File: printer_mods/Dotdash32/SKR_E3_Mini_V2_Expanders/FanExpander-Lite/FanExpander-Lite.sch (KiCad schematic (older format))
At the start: 31 parts, among them J1 FAN1, J2 FAN2, J3 FAN3, J4 FAN4, J5 EXP1_IN, J6 FAN1_IN, J7 IO_PassThrough, Q1 IRLML6344, Q2 IRLML6344, Q3 IRLML6344

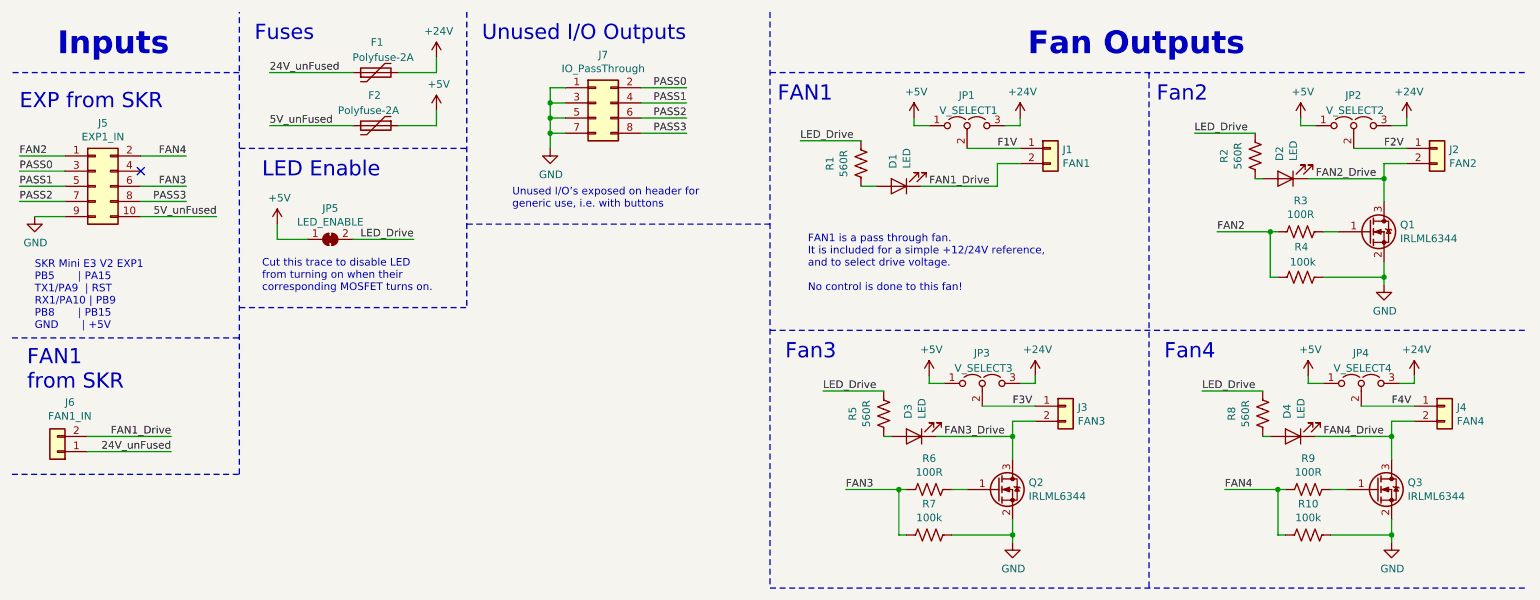
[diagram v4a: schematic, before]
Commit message: feat: trim outline to not collide with TH exp
also some fun little changes for internal structure
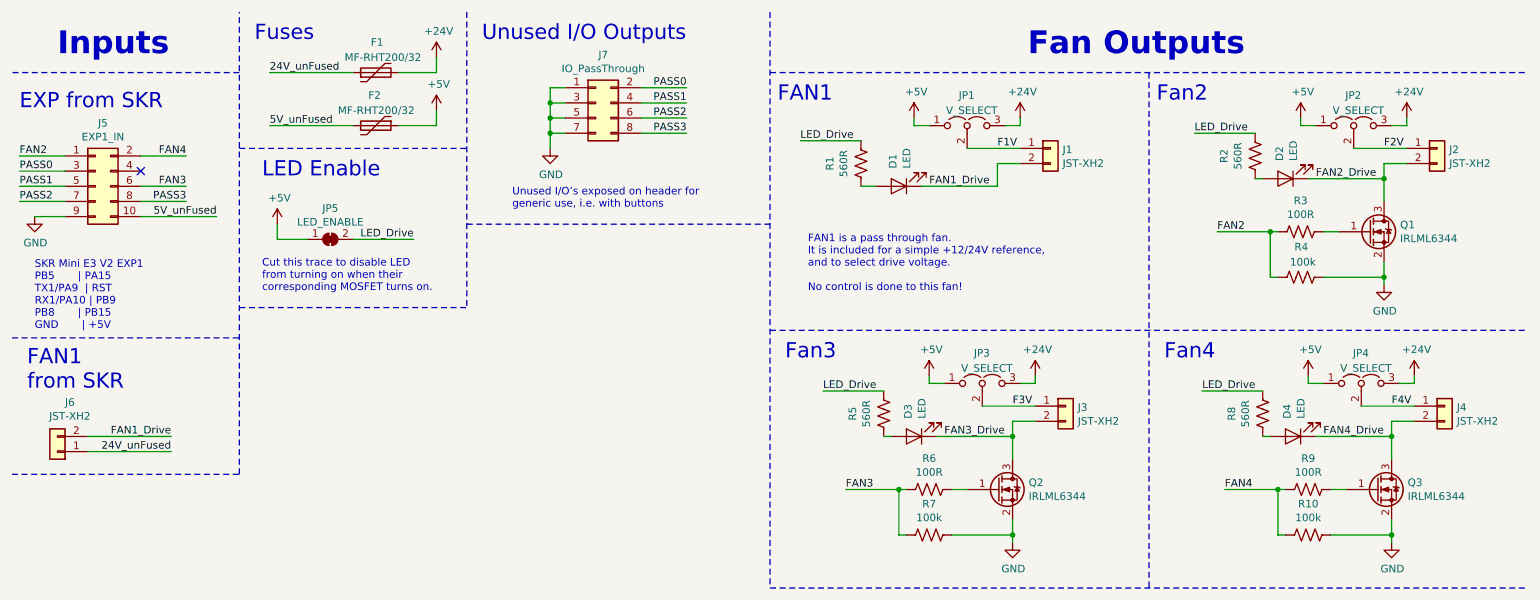
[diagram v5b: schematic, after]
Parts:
- F1, F2: value Polyfuse-2A -> MF-RHT200/32
- J1: value FAN1 -> JST-XH2
- J2: value FAN2 -> JST-XH2
- J3: value FAN3 -> JST-XH2
- J4: value FAN4 -> JST-XH2
- J6: value FAN1_IN -> JST-XH2
- JP1: value V_SELECT1 -> V_SELECT
- JP2: value V_SELECT2 -> V_SELECT
- JP3: value V_SELECT3 -> V_SELECT
- JP4: value V_SELECT4 -> V_SELECT
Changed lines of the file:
@@
 Sheet 1 1
 Title "SKR E3 Mini Fan Expander Lite"
-Date "2021-12-18"
-Rev "V0.1.1"
+Date "2022-01-05"
+Rev "V1.0.1"
 Comp "Voron Design"
 Comment1 "Drawn by Dotdash32 (JDeW)"
@@
 P 800 3400
 F 0 "J6" H 718 3075 50  0000 C CNN
-F 1 "FAN1_IN" H 718 3166 50  0000 C CNN
+F 1 "JST-XH2" H 718 3166 50  0000 C CNN
 F 2 "Connectors_JST:JST_XH_B02B-XH-A_02x2.50mm_Straight" H 800 3400 50  0001 C CNN
 F 3 "~" H 800 3400 50  0001 C CNN
@@
 P 2900 900
 F 0 "F1" V 3100 850 50  0000 L CNN
-F 1 "Polyfuse-2A" V 3000 650 50  0000 L CNN
+F 1 "MF-RHT200/32" V 3000 600 50  0000 L CNN
 F 2 "Fuse:Fuse_Bourns_MF-RHT200" H 2950 700 50  0001 L CNN
 F 3 "~" H 2900 900 50  0001 C CNN
@@
 P 7350 1400
 F 0 "J1" H 7430 1392 50  0000 L CNN
-F 1 "FAN1" H 7430 1301 50  0000 L CNN
+F 1 "JST-XH2" H 7430 1301 50  0000 L CNN
 F 2 "Connectors_JST:JST_XH_B02B-XH-A_02x2.50mm_Straight" H 7350 1400 50  0001 C CNN
 F 3 "~" H 7350 1400 50  0001 C CNN
@@
 P 6800 1250
 F 0 "JP1" H 6850 1450 50  0000 R CNN
-F 1 "V_SELECT1" H 7000 1350 50  0000 R CNN
+F 1 "V_SELECT" H 7000 1350 50  0000 R CNN
 F 2 "Pin_Headers:Pin_Header_Straight_1x03_Pitch2.54mm" H 6800 1250 50  0001 C CNN
 F 3 "~" H 6800 1250 50  0001 C CNN
@@
 P 9900 1400
 F 0 "J2" H 9980 1392 50  0000 L CNN
-F 1 "FAN2" H 9980 1301 50  0000 L CNN
+F 1 "JST-XH2" H 9980 1301 50  0000 L CNN
 F 2 "Connectors_JST:JST_XH_B02B-XH-A_02x2.50mm_Straight" H 9900 1400 50  0001 C CNN
 F 3 "~" H 9900 1400 50  0001 C CNN
@@
 P 9350 1250
 F 0 "JP2" H 9400 1450 50  0000 R CNN
-F 1 "V_SELECT2" H 9550 1350 50  0000 R CNN
+F 1 "V_SELECT" H 9550 1350 50  0000 R CNN
 F 2 "Pin_Headers:Pin_Header_Straight_1x03_Pitch2.54mm" H 9350 1250 50  0001 C CNN
 F 3 "~" H 9350 1250 50  0001 C CNN
@@
 P 7450 3100
 F 0 "J3" H 7530 3092 50  0000 L CNN
-F 1 "FAN3" H 7530 3001 50  0000 L CNN
+F 1 "JST-XH2" H 7530 3001 50  0000 L CNN
 F 2 "Connectors_JST:JST_XH_B02B-XH-A_02x2.50mm_Straight" H 7450 3100 50  0001 C CNN
 F 3 "~" H 7450 3100 50  0001 C CNN
@@
 P 6900 2950
 F 0 "JP3" H 6950 3150 50  0000 R CNN
-F 1 "V_SELECT3" H 7100 3050 50  0000 R CNN
+F 1 "V_SELECT" H 7100 3050 50  0000 R CNN
 F 2 "Pin_Headers:Pin_Header_Straight_1x03_Pitch2.54mm" H 6900 2950 50  0001 C CNN
 F 3 "~" H 6900 2950 50  0001 C CNN
@@
 P 9950 3100
 F 0 "J4" H 10030 3092 50  0000 L CNN
-F 1 "FAN4" H 10030 3001 50  0000 L CNN
+F 1 "JST-XH2" H 10030 3001 50  0000 L CNN
 F 2 "Connectors_JST:JST_XH_B02B-XH-A_02x2.50mm_Straight" H 9950 3100 50  0001 C CNN
 F 3 "~" H 9950 3100 50  0001 C CNN
@@
 P 9400 2950
 F 0 "JP4" H 9450 3150 50  0000 R CNN
-F 1 "V_SELECT4" H 9600 3050 50  0000 R CNN
+F 1 "V_SELECT" H 9600 3050 50  0000 R CNN
 F 2 "Pin_Headers:Pin_Header_Straight_1x03_Pitch2.54mm" H 9400 2950 50  0001 C CNN
 F 3 "~" H 9400 2950 50  0001 C CNN
@@
 P 2900 1250
 F 0 "F2" V 2700 1200 50  0000 L CNN
-F 1 "Polyfuse-2A" V 2800 1000 50  0000 L CNN
+F 1 "MF-RHT200/32" V 2800 1000 50  0000 L CNN
 F 2 "Fuse:Fuse_Bourns_MF-RHT200" H 2950 1050 50  0001 L CNN
 F 3 "~" H 2900 1250 50  0001 C CNN

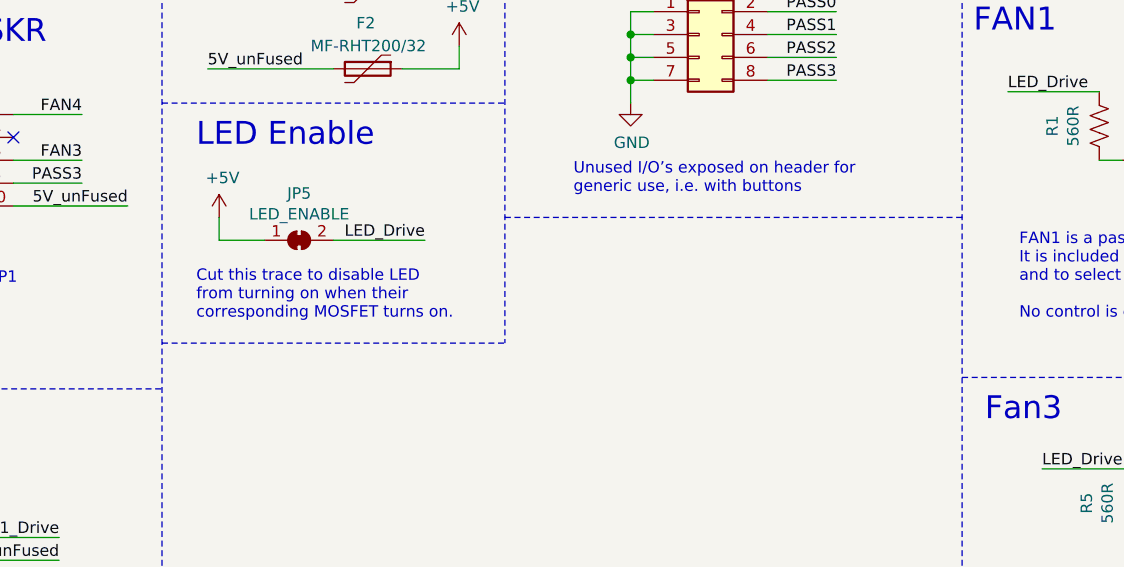
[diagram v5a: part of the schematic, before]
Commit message: feat: add LCSC bom, add alignment fiducials
redoing some BOM stuff, oh how i hate BOM management
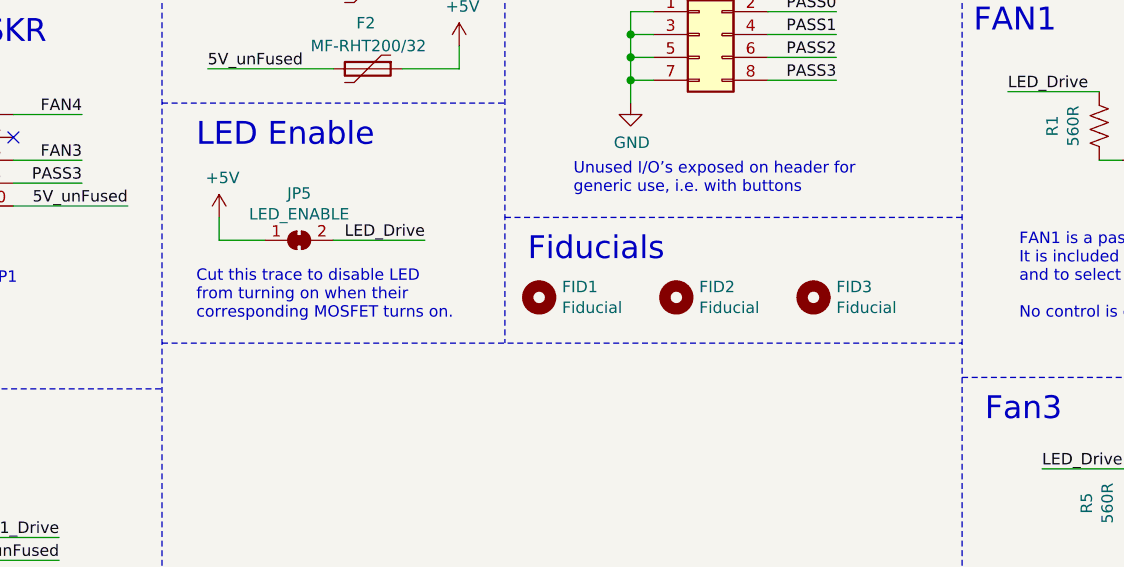
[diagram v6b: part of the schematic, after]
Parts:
- added FID1, FID2, FID3: Fiducial, Fiducials:Fiducial_0.5mm_Dia_1mm_Outer, symbol Mechanical:MountingHole
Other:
- note added: "Fiducials"
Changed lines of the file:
@@
 Sheet 1 1
 Title "SKR E3 Mini Fan Expander Lite"
-Date "2022-01-05"
-Rev "V1.0.1"
+Date "2022-01-10"
+Rev "V1.0.2"
 Comp "Voron Design"
 Comment1 "Drawn by Dotdash32 (JDeW)"
@@
 Cut this trace to disable LED\nfrom turning on when their\ncorresponding MOSFET turns on.
 Wire Notes Line
-	2000 2450 3500 2450
-Wire Notes Line
 	3500 500  3500 2450
 $Comp
@@
 Wire Notes Line
 	3500 1900 5500 1900
+$Comp
+L Mechanical:MountingHole FID1
+U 1 1 61DD8A6E
+P 3650 2250
+F 0 "FID1" H 3750 2296 50  0000 L CNN
+F 1 "Fiducial" H 3750 2205 50  0000 L CNN
+F 2 "Fiducials:Fiducial_0.5mm_Dia_1mm_Outer" H 3650 2250 50  0001 C CNN
+F 3 "~" H 3650 2250 50  0001 C CNN
+	1    3650 2250
+	1    0    0    -1
+$EndComp
+$Comp
+L Mechanical:MountingHole FID2
+U 1 1 61DDDD44
+P 4250 2250
+F 0 "FID2" H 4350 2296 50  0000 L CNN
+F 1 "Fiducial" H 4350 2205 50  0000 L CNN
+F 2 "Fiducials:Fiducial_0.5mm_Dia_1mm_Outer" H 4250 2250 50  0001 C CNN
+F 3 "~" H 4250 2250 50  0001 C CNN
+	1    4250 2250
+	1    0    0    -1
+$EndComp
+$Comp
+L Mechanical:MountingHole FID3
+U 1 1 61DE12C9
+P 4850 2250
+F 0 "FID3" H 4950 2296 50  0000 L CNN
+F 1 "Fiducial" H 4950 2205 50  0000 L CNN
+F 2 "Fiducials:Fiducial_0.5mm_Dia_1mm_Outer" H 4850 2250 50  0001 C CNN
+F 3 "~" H 4850 2250 50  0001 C CNN
+	1    4850 2250
+	1    0    0    -1
+$EndComp
+Wire Notes Line
+	2000 2450 5500 2450
+Text Notes 3600 2100 0    100  ~ 0
+Fiducials
 $EndSCHEMATC

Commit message: fix: update reverse LED mounts at SCH level
were using the wrong hole pattern, not big enough!!
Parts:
- D1, D2, D3, D4: footprint LED_SMD:LED_1206_3216Metric_ReverseMount_Hole1.8x2.4mm -> LED_SMD:LED_1206_3216Metric_ReverseMount_Hole2.1x2.1mm
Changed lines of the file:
@@
 Title "SKR E3 Mini Fan Expander Lite"
 Date "2022-01-10"
-Rev "V1.0.2"
+Rev "V1.0.3"
 Comp "Voron Design"
 Comment1 "Drawn by Dotdash32 (JDeW)"
@@
 F 0 "D2" V 8939 1483 50  0000 R CNN
 F 1 "LED" V 8848 1483 50  0000 R CNN
-F 2 "LED_SMD:LED_1206_3216Metric_ReverseMount_Hole1.8x2.4mm" H 8900 1600 50  0001 C CNN
+F 2 "LED_SMD:LED_1206_3216Metric_ReverseMount_Hole2.1x2.1mm" H 8900 1600 50  0001 C CNN
 F 3 "~" H 8900 1600 50  0001 C CNN
 	1    8900 1600
@@
 F 0 "D1" V 6389 1533 50  0000 R CNN
 F 1 "LED" V 6298 1533 50  0000 R CNN
-F 2 "LED_SMD:LED_1206_3216Metric_ReverseMount_Hole1.8x2.4mm" H 6350 1650 50  0001 C CNN
+F 2 "LED_SMD:LED_1206_3216Metric_ReverseMount_Hole2.1x2.1mm" H 6350 1650 50  0001 C CNN
 F 3 "~" H 6350 1650 50  0001 C CNN
 	1    6350 1650
@@
 F 0 "D3" V 6489 3183 50  0000 R CNN
 F 1 "LED" V 6398 3183 50  0000 R CNN
-F 2 "LED_SMD:LED_1206_3216Metric_ReverseMount_Hole1.8x2.4mm" H 6450 3300 50  0001 C CNN
+F 2 "LED_SMD:LED_1206_3216Metric_ReverseMount_Hole2.1x2.1mm" H 6450 3300 50  0001 C CNN
 F 3 "~" H 6450 3300 50  0001 C CNN
 	1    6450 3300
@@
 F 0 "D4" V 8989 3183 50  0000 R CNN
 F 1 "LED" V 8898 3183 50  0000 R CNN
-F 2 "LED_SMD:LED_1206_3216Metric_ReverseMount_Hole1.8x2.4mm" H 8950 3300 50  0001 C CNN
+F 2 "LED_SMD:LED_1206_3216Metric_ReverseMount_Hole2.1x2.1mm" H 8950 3300 50  0001 C CNN
 F 3 "~" H 8950 3300 50  0001 C CNN
 	1    8950 3300

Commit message: feat: solder paste filled jumpers
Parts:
- JP5: footprint Jumper:SolderJumper-2_P1.3mm_Bridged_RoundedPad1.0x1.5mm -> Jumper:SolderJumper-2_P1.3mm_Pasted_RoundedPad1.0x1.5mm
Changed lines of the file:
@@
 Sheet 1 1
 Title "SKR E3 Mini Fan Expander Lite"
-Date "2022-01-10"
-Rev "V1.0.3"
+Date "2022-01-16"
+Rev "V1.0.4"
 Comp "Voron Design"
 Comment1 "Drawn by Dotdash32 (JDeW)"
@@
 F 0 "JP5" H 2600 2205 50  0000 C CNN
 F 1 "LED_ENABLE" H 2600 2114 50  0000 C CNN
-F 2 "Jumper:SolderJumper-2_P1.3mm_Bridged_RoundedPad1.0x1.5mm" H 2600 2000 50  0001 C CNN
+F 2 "Jumper:SolderJumper-2_P1.3mm_Pasted_RoundedPad1.0x1.5mm" H 2600 2000 50  0001 C CNN
 F 3 "~" H 2600 2000 50  0001 C CNN
 	1    2600 2000
